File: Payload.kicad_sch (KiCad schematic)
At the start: 13 parts, among them U1 STM32-(STM32H745ZIT6)

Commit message: Schematic fini, en théorie
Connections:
- net ADC2_PC0 is gone; now on an unnamed net: R18.1
- net GND: now also U1.29 (PC1), U1.44 (PA5); no longer U1.1 (PE2), U1.10 (PC14-OSC32_IN), U1.108 (PA15), U1.109 (PC10), U1.11 (PC15-OSC32_OUT), U1.110 (PC11), U1.111 (PC12), U1.112 (PD0), U1.113 (PD1), U1.114 (PD2), U1.115 (PD3), U1.116 (PD4), U1.117 (PD5), U1.120 (PD6), U1.121 (PD7), U1.122 (PG9), U1.123 (PG10), U1.124 (PG11), U1.125 (PG12), U1.126 (PG13), U1.127 (PG14), U1.131 (PB4), U1.132 (PB5), U1.133 (PB6), U1.134 (PB7), U1.136 (PB8), U1.137 (PB9), U1.138 (PE0), U1.139 (PE1), U1.2 (PE3), U1.20 (PF6), U1.22 (PF8), U1.24 (PF10), U1.25 (PH0-OSC_IN), U1.26 (PH1-OSC_OUT), U1.3 (PE4), U1.31 (PC3_C), U1.37 (PA0), U1.39 (PA2), U1.4 (PE5), U1.40 (PA3), U1.43 (PA4), U1.45 (PA6), U1.47 (PC4), U1.48 (PC5), U1.49 (PB0), U1.5 (PE6), U1.51 (PB2), U1.53 (PF14), U1.54 (PF15), U1.63 (PE13), U1.64 (PE14), U1.65 (PE15), U1.66 (PB10), U1.67 (PB11), U1.72 (PB12), U1.73 (PB13), U1.74 (PB14), U1.75 (PB15), U1.76 (PD8), U1.77 (PD9), U1.78 (PD10), U1.81 (PD11), U1.86 (PG6), U1.87 (PG7), U1.88 (PG8), U1.9 (PC13), U1.93 (PC6), U1.94 (PC7), U1.95 (PC8), U1.96 (PC9), U1.97 (PA8), U1.98 (PA9)
- net MISO: now also U1.74 (PB14); no longer U1.84 (PD14)
- net at R14.2: now also U1.45 (PA6); no longer U1.23 (PF9)
- net at R24.2: now also U1.75 (PB15); no longer U1.85 (PD15)
- net at U1.28 (PC0): no longer R18.2
- net ADC12_INP14-SG1.2: now reaches R10.2
- net ADC12_INP14-SG1.2: no longer U1.21 (PF7)
- net at U1.52 (PF11): no longer R19.2
- net ADC12_INP15-SG3.4: now reaches R21.2
- net ADC12_INP15-SG3.4: no longer U1.29 (PC1)
- net at R9.2: now also U1.37 (PA0); no longer U1.50 (PB1)
- net at R12.2: now also U1.43 (PA4); no longer U1.44 (PA5)
- net at R22.2: now also U1.72 (PB12); no longer U1.82 (PD12)
- net at R23.2: now also U1.73 (PB13); no longer U1.83 (PD13)
- net ADC1_PA5 renamed ADC12_INP18-SG5.6
- net ADC1_PB1 renamed ADC1_INP16-Therm2
- net ADC1_PF11: no longer names the net of R19.1
- net ADC1_PF11: now also U1.31 (PC3_C)
- net ADC2_PC1: no longer names the net of R21.1
- net ADC2_PC1: now also U1.40 (PA3)
- net ADC3_PF7 : no longer names the net of R10.1
- net ADC3_PF7 : now also U1.39 (PA2)
- net ADC3_PF9  renamed ADC12_INP3-Therm1
- net QUAD_IO0 renamed QUADSPI_BK2_IO0
- net QUAD_IO1 renamed QUADSPI_BK2_IO1
- net QUAD_IO2 renamed QUADSPI_BK2_IO2
- net QUAD_IO3 renamed QUADSPI_BK2_IO3
- net QUAD_NSS: no longer names the net of U1.61 (PE11)
- net QUAD_SCK: no longer names the net of U1.62 (PE12)
- new net ADC123_INP10-Vibro2: R18.2
- new net ADC3_INP1-Vibe1: R19.2
- new net InteruptionMPU: U1.67 (PB11)
- new net QUADSPI_BK1_IO0: U1.22 (PF8)
- new net QUADSPI_BK1_IO1: U1.23 (PF9)
- new net QUADSPI_BK1_IO2: U1.21 (PF7)
- new net QUADSPI_BK1_IO3: U1.20 (PF6)
- new net QUADSPI_BK1_NCS: U1.66 (PB10)
- new net QUADSPI_BK2_NCS: U1.110 (PC11)
- new net QUADSPI_CLK: U1.24 (PF10)
- no-connect marks 1 -> 66
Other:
- note added: ")-entrée diff"
- note added: "ADC 1: thermistances"
- note added: "ADC 2: strain gauge"
- note added: "ADC3: vibromètres"
- note added: "entrée diff-("
- note removed: "<--Analog"
- note removed: "ADC 1: PF11, PB1, PA5 pour les strain gauge"
- note removed: "ADC 2: PC0 PC1 pour les thermistances"
- note removed: "ADC3: PF7 et PF9 pour vibromètres"
- note removed: "PE7: IO0, PE8: IO1, PE9: IO2, PE10: IO3, PE11: NSS, PE12: SCK du quadSPI"
- moved on the sheet: R26, U1B

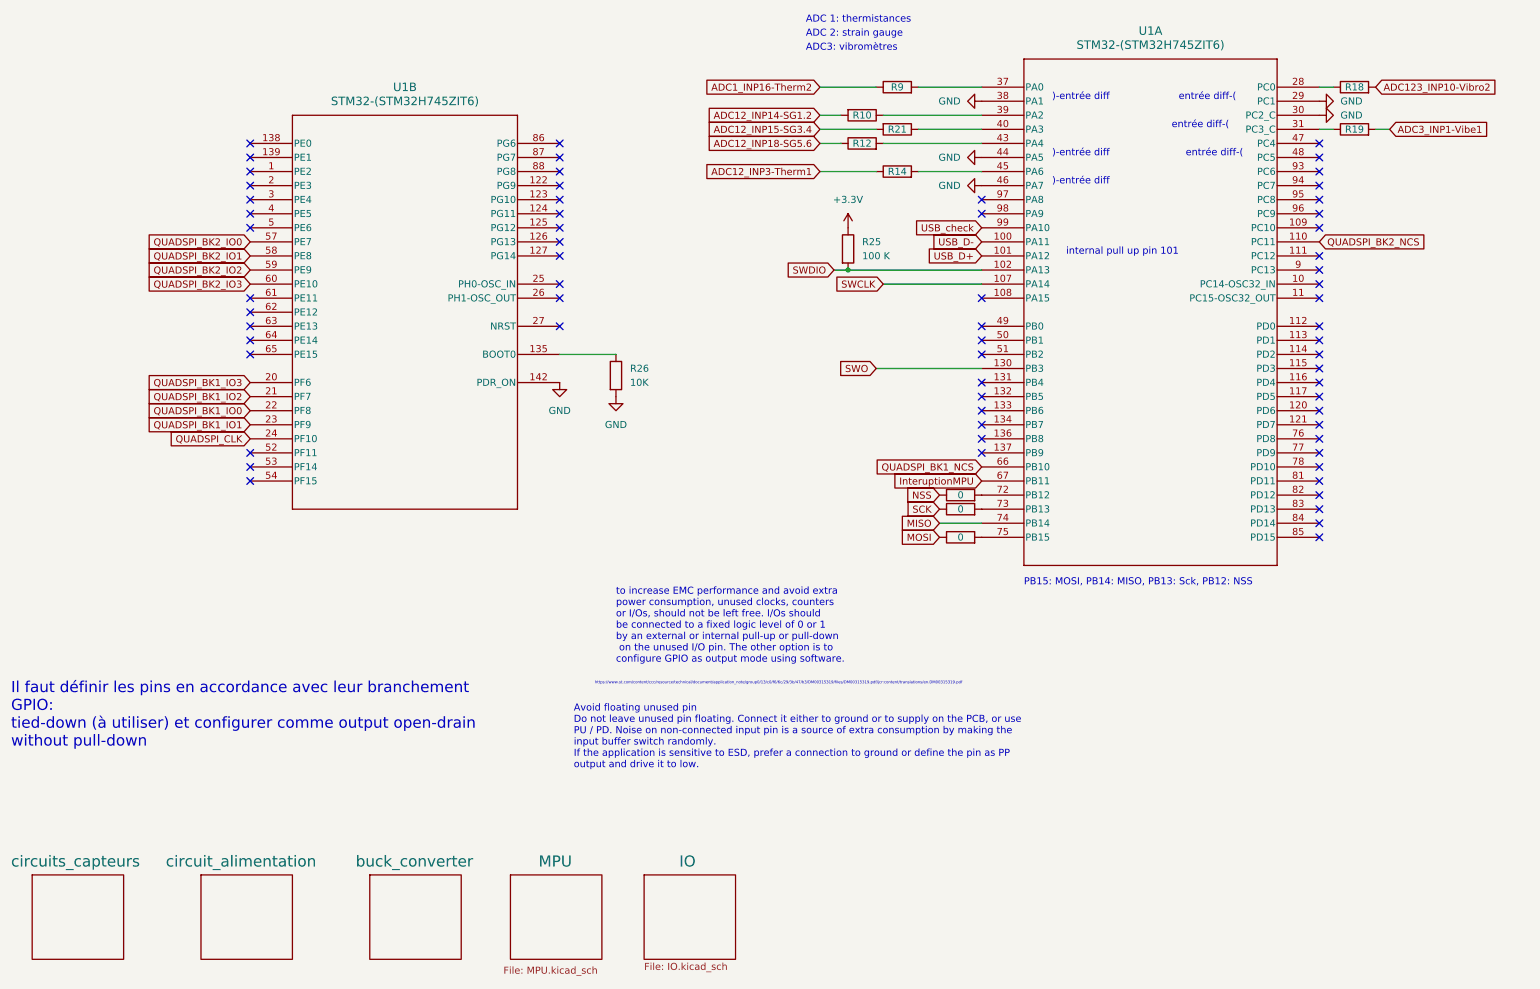
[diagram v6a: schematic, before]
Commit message: Petites modif et assignation des empreintes à 50%
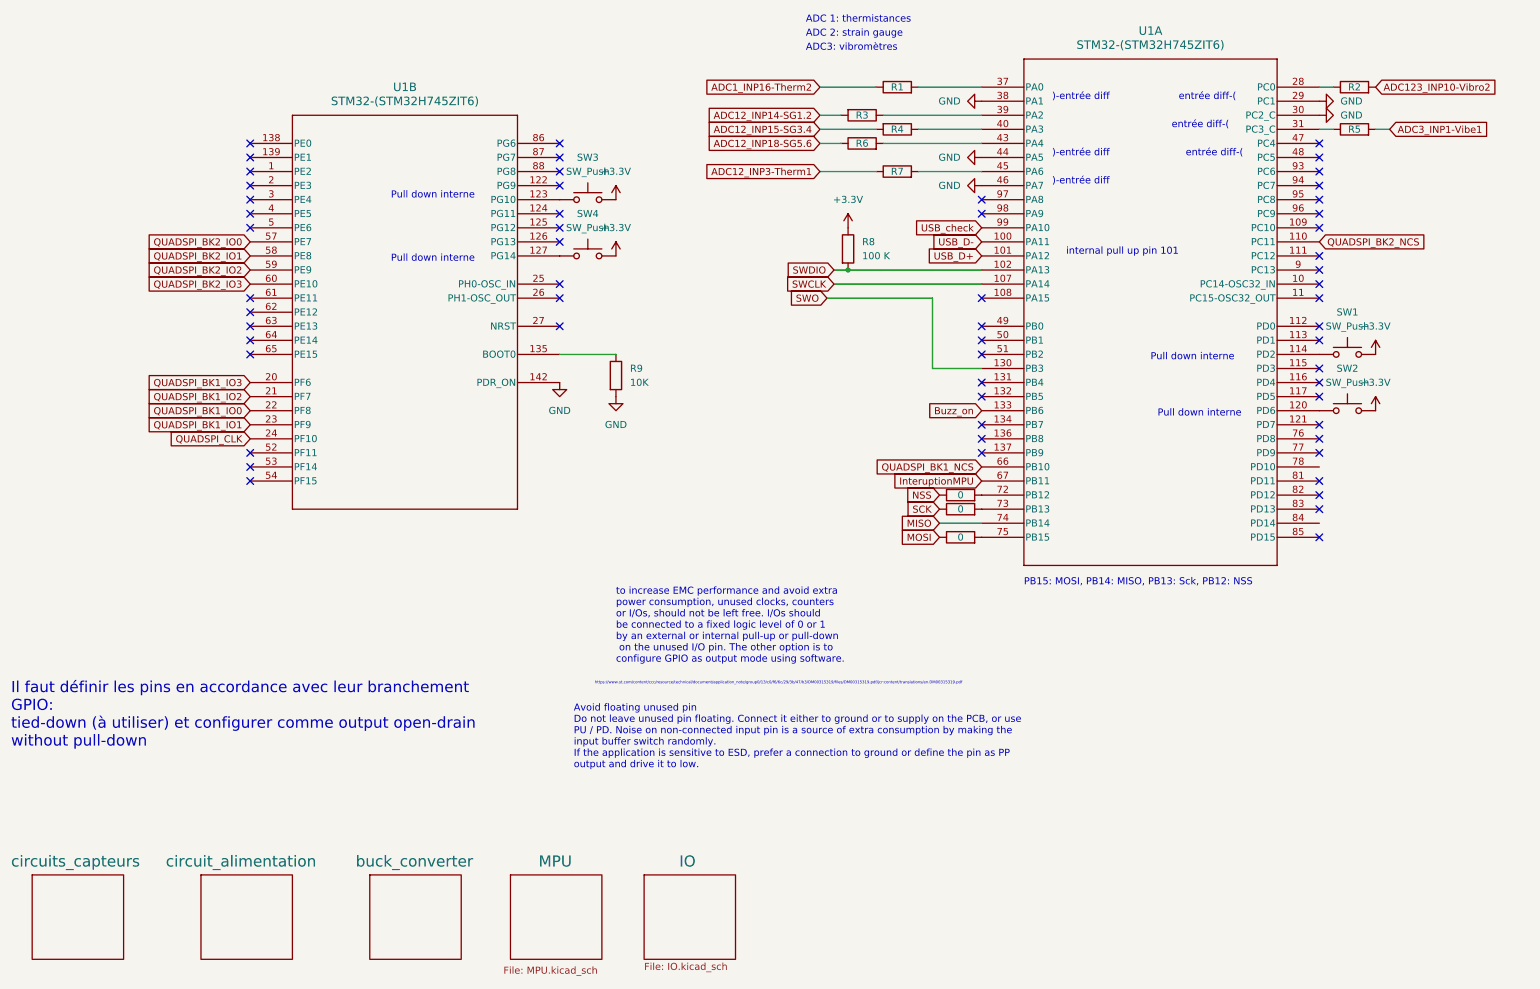
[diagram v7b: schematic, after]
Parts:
- added SW1, SW2, SW3, SW4: SW_Push, GAUL-Empreintes:bouton-(SW_TS02-66-60-BK-160-LCR-D), symbol Switch:SW_Push
- R1: renamed from R9; footprint (none) -> Resistor_SMD:R_0603_1608Metric
- R10: renamed from R22; footprint (none) -> Resistor_SMD:R_0603_1608Metric
- R11: renamed from R23; footprint (none) -> Resistor_SMD:R_0603_1608Metric
- R12: renamed from R24; footprint (none) -> Resistor_SMD:R_0603_1608Metric
- R2: renamed from R18; footprint (none) -> Resistor_SMD:R_0603_1608Metric
- R3: renamed from R10; footprint (none) -> Resistor_SMD:R_0603_1608Metric
- R4: renamed from R21; footprint (none) -> Resistor_SMD:R_0603_1608Metric
- R5: renamed from R19; footprint (none) -> Resistor_SMD:R_0603_1608Metric
- R6: renamed from R12; footprint (none) -> Resistor_SMD:R_0603_1608Metric
- R7: renamed from R14; footprint (none) -> Resistor_SMD:R_0603_1608Metric
- R8: renamed from R25; footprint (none) -> Resistor_SMD:R_0603_1608Metric
- R9: renamed from R26; footprint (none) -> Resistor_SMD:R_0603_1608Metric
- U1: footprint LQFP-144 -> GAUL-Empreintes:STM32
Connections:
- net +3.3V: now also SW1.4, SW2.4, SW3.4, SW4.4
- net at U1.123 (PG10): now also SW3.1
- net at U1.127 (PG14): now also SW4.1
- net at U1.114 (PD2): now also SW1.1
- net at U1.120 (PD6): now also SW2.1
- net Buzz_on: now reaches U1.133 (PB6)
- no-connect marks 66 -> 59
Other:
- note added: "Pull down interne"

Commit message: Début PCB
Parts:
- removed SW3, SW4: SW_Push, GAUL-Empreintes:bouton-(SW_TS02-66-60-BK-160-LCR-D), symbol Switch:SW_Push
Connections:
- no-connect marks 59 -> 63
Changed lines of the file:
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@@
   (junction (at 165.1 67.31) (diameter 0) (color 0 0 0 0)
   )
+  (no_connect (at 113.03 64.77))
   (no_connect (at 189.23 80.01))
   (no_connect (at 57.15 54.61))
   (no_connect (at 57.15 57.15))
   (no_connect (at 189.23 90.17))
+  (no_connect (at 250.19 113.03))
   (no_connect (at 250.19 97.79))
   (no_connect (at 250.19 44.45))
@@
   (no_connect (at 250.19 107.95))
   (no_connect (at 113.03 69.85))
+  (no_connect (at 113.03 54.61))
   (no_connect (at 250.19 115.57))
   (no_connect (at 113.03 57.15))
@@
   (no_connect (at 250.19 69.85))
   (no_connect (at 57.15 72.39))
+  (no_connect (at 250.19 102.87))
   (no_connect (at 250.19 110.49))
   (wire (pts (xy 177.8 49.53) (xy 189.23 49.53))
@@
     )
   )
-  (symbol (lib_id "power:+3.3V") (at 123.19 64.77 0) (unit 1)
-    (in_bom yes) (on_board yes) (dnp no) (fields_autoplaced)
-    (property "Reference" "#PWR?" (at 123.19 68.58 0)
-      (effects (font (size 1.27 1.27)) hide)
-    )
-    (property "Value" "+3.3V" (at 123.19 59.69 0)
-      (effects (font (size 1.27 1.27)))
-    )
-    (property "Footprint" "" (at 123.19 64.77 0)
-      (effects (font (size 1.27 1.27)) hide)
-    )
-    (property "Datasheet" "" (at 123.19 64.77 0)
-      (effects (font (size 1.27 1.27)) hide)
-    )
-    (pin "1")
-    (instances
-      (project "Payload"
-        (path "/5f62c44b-34ee-4720-b187-b4a520863a8a/b20c1a40-233f-480d-ac91-6f1a7bcdc93c"
-          (reference "#PWR?") (unit 1)
-        )
-        (path "/5f62c44b-34ee-4720-b187-b4a520863a8a"
-          (reference "#PWR0137") (unit 1)
-        )
-      )
-    )
-  )
   (symbol (lib_id "Device:R") (at 167.64 44.45 90) (unit 1)
     (in_bom yes) (on_board yes) (dnp no)
@@
     )
   )
-  (symbol (lib_name "SW_Push_2") (lib_id "Switch:SW_Push") (at 118.11 64.77 0) (unit 1)
-    (in_bom yes) (on_board yes) (dnp no) (fields_autoplaced)
-    (property "Reference" "SW4" (at 118.11 57.15 0)
-      (effects (font (size 1.27 1.27)))
-    )
-    (property "Value" "SW_Push" (at 118.11 59.69 0)
-      (effects (font (size 1.27 1.27)))
-    )
-    (property "Footprint" "GAUL-Empreintes:bouton-(SW_TS02-66-60-BK-160-LCR-D)" (at 118.11 59.69 0)
-      (effects (font (size 1.27 1.27)) hide)
-    )
-    (property "Datasheet" "~" (at 118.11 59.69 0)
-      (effects (font (size 1.27 1.27)) hide)
-    )
-    (pin "1")
-    (pin "4")
-    (instances
-      (project "Payload"
-        (path "/5f62c44b-34ee-4720-b187-b4a520863a8a"
-          (reference "SW4") (unit 1)
-        )
-      )
-    )
-  )
   (symbol (lib_id "power:GND") (at 250.19 39.37 90) (unit 1)
     (in_bom yes) (on_board yes) (dnp no) (fields_autoplaced)
@@
         (path "/5f62c44b-34ee-4720-b187-b4a520863a8a"
           (reference "R12") (unit 1)
-        )
-      )
-    )
-  )
-  (symbol (lib_name "SW_Push_1") (lib_id "Switch:SW_Push") (at 118.11 54.61 0) (unit 1)
-    (in_bom yes) (on_board yes) (dnp no) (fields_autoplaced)
-    (property "Reference" "SW3" (at 118.11 46.99 0)
-      (effects (font (size 1.27 1.27)))
-    )
-    (property "Value" "SW_Push" (at 118.11 49.53 0)
-      (effects (font (size 1.27 1.27)))
-    )
-    (property "Footprint" "GAUL-Empreintes:bouton-(SW_TS02-66-60-BK-160-LCR-D)" (at 118.11 49.53 0)
-      (effects (font (size 1.27 1.27)) hide)
-    )
-    (property "Datasheet" "~" (at 118.11 49.53 0)
-      (effects (font (size 1.27 1.27)) hide)
-    )
-    (pin "1")
-    (pin "4")
-    (instances
-      (project "Payload"
-        (path "/5f62c44b-34ee-4720-b187-b4a520863a8a"
-          (reference "SW3") (unit 1)
         )
       )
@@
         )
       )
-    )
-  )
-  (symbol (lib_id "power:+3.3V") (at 123.19 54.61 0) (unit 1)
-    (in_bom yes) (on_board yes) (dnp no) (fields_autoplaced)
-    (property "Reference" "#PWR?" (at 123.19 58.42 0)
-      (effects (font (size 1.27 1.27)) hide)
-    )
-    (property "Value" "+3.3V" (at 123.19 49.53 0)
-      (effects (font (size 1.27 1.27)))
-    )
-    (property "Footprint" "" (at 123.19 54.61 0)
-      (effects (font (size 1.27 1.27)) hide)
-    )
-    (property "Datasheet" "" (at 123.19 54.61 0)
-      (effects (font (size 1.27 1.27)) hide)
-    )
-    (pin "1")
-    (instances
-      (project "Payload"
-        (path "/5f62c44b-34ee-4720-b187-b4a520863a8a/b20c1a40-233f-480d-ac91-6f1a7bcdc93c"
-          (reference "#PWR?") (unit 1)
-        )
-        (path "/5f62c44b-34ee-4720-b187-b4a520863a8a"
-          (reference "#PWR0136") (unit 1)
-        )
-      )
